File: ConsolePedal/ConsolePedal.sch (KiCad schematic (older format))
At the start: 1 part, among them U1 N64-Cartridge

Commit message: Finished schematic
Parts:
- added BT1: Battery, symbol Device:Battery
- added D1: LED, LED_THT:LED_D5.0mm, symbol Device:LED
- added J1: AudioJack3, Connector_PinSocket_2.54mm:PinSocket_1x03_P2.54mm_Vertical, symbol audioJacks:AudioJack3
- added J2: AudioJack2, Connector_PinSocket_2.54mm:PinSocket_1x02_P2.54mm_Vertical, symbol audioJacks:AudioJack2
- added R1: R, Resistor_THT:R_Axial_DIN0207_L6.3mm_D2.5mm_P10.16mm_Horizontal, symbol Device:R
- added S1: SWITCH-3PDT-PTH-STOMP, MuffPi:STOMP_SWITCH_3PDT, symbol SparkFun-Switches:SWITCH-3PDT-PTH-STOMP
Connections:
- net GND: now reaches U1.1 (GND)
- net GND: now also U1.2 (GND), U1.49 (RAUDIO), U1.50 (GND), J1.1, J2.2, R1.2
- net Input: now reaches U1.3 (AD15)
- net Input: now also U1.48 (GND), S1.P$3 (S)
- net Output: now reaches U1.4 (AD14)
- net Output: now also U1.47 (GND), S1.P$6 (S)
- net LEDPower: now reaches U1.45 (os_event_cart)
- net LEDPower: now also U1.6 (GND), D1.2 (A), S1.P$9 (S)
- net +9V: now reaches U1.46 (NC)
- net +9V: now also U1.5 (AD13), BT1.1 (+), S1.P$8 (P)
- new net: J2.1, S1.P$5 (P)
- new net: BT1.2 (-), J1.2
- new net: J1.3, S1.P$2 (P)
- new net: S1.P$1 (O), S1.P$4 (O)
- new net: D1.1 (K), R1.1
- no-connect marks 0 -> 1
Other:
- moved on the sheet: U1

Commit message: Finalized board layout. Working on pcb graphics
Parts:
- removed U1: N64-Cartridge, Connector_PinSocket_2.54mm:PinSocket_2x25_P2.54mm_Vertical, symbol n64-cartridge:N64-Cartridge
- added J3: Conn_02x25_Odd_Even, Connector_PinSocket_2.54mm:PinSocket_2x25_P2.54mm_Vertical, symbol Connector_Generic:Conn_02x25_Odd_Even
- BT1: footprint (none) -> Connector_PinSocket_2.54mm:PinSocket_1x02_P2.54mm_Vertical
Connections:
- net +9V: now also J3.10 (Pin_10), J3.41 (Pin_41), J3.42 (Pin_42), J3.9 (Pin_9)
- net GND: now also J3.1 (Pin_1), J3.2 (Pin_2), J3.3 (Pin_3), J3.4 (Pin_4), J3.47 (Pin_47), J3.48 (Pin_48), J3.49 (Pin_49), J3.50 (Pin_50)
- net Input: now also J3.45 (Pin_45), J3.46 (Pin_46), J3.5 (Pin_5), J3.6 (Pin_6)
- net LEDPower: now also J3.11 (Pin_11), J3.12 (Pin_12), J3.39 (Pin_39), J3.40 (Pin_40)
- net Output: now also J3.43 (Pin_43), J3.44 (Pin_44), J3.7 (Pin_7), J3.8 (Pin_8)
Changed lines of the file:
@@
 F 0 "BT1" H 5458 1696 50  0000 L CNN
 F 1 "Battery" H 5458 1605 50  0000 L CNN
-F 2 "" V 5350 1710 50  0001 C CNN
+F 2 "Connector_PinSocket_2.54mm:PinSocket_1x02_P2.54mm_Vertical" V 5350 1710 50  0001 C CNN
 F 3 "~" V 5350 1710 50  0001 C CNN
 	1    5350 1650
@@
 	8250 1550 8250 1650
 $Comp
-L power:GND #PWR09
-U 1 1 5FA91B35
-P 10450 3950
-F 0 "#PWR09" H 10450 3700 50  0001 C CNN
-F 1 "GND" H 10455 3777 50  0000 C CNN
-F 2 "" H 10450 3950 50  0001 C CNN
-F 3 "" H 10450 3950 50  0001 C CNN
-	1    10450 3950
-	1    0    0    -1
-$EndComp
-Wire Wire Line
-	10300 3950 10450 3950
-Wire Wire Line
-	10300 3850 10300 3950
-$Comp
 L power:GND #PWR06
 U 1 1 5FA92668
@@
 Wire Wire Line
 	7650 1550 8250 1550
-Text Label 10300 3750 0    50   ~ 0
-Input
-Text Label 10300 3650 0    50   ~ 0
-Output
 Text Label 8250 1750 2    50   ~ 0
 Input
@@
 	0    -1   -1   0
 $EndComp
-$Comp
-L power:+9V #PWR08
-U 1 1 5FA963AA
-P 10300 3550
-F 0 "#PWR08" H 10300 3400 50  0001 C CNN
-F 1 "+9V" V 10315 3678 50  0000 L CNN
-F 2 "" H 10300 3550 50  0001 C CNN
-F 3 "" H 10300 3550 50  0001 C CNN
-	1    10300 3550
-	0    1    1    0
-$EndComp
 Text Label 6800 3150 0    50   ~ 0
 LEDPower
@@
 Text Label 8250 2050 2    50   ~ 0
 LEDPower
-Text Label 10300 3450 0    50   ~ 0
+Text Label 8750 3450 0    50   ~ 0
 LEDPower
-Connection ~ 10300 3950
-Connection ~ 8250 1550
 $Comp
-L n64-cartridge:N64-Cartridge U1
-U 1 1 5FA742E9
-P 9300 3850
-F 0 "U1" H 9300 6350 60  0000 C CNN
-F 1 "N64-Cartridge" H 9300 6450 60  0000 C CNN
-F 2 "Connector_PinSocket_2.54mm:PinSocket_2x25_P2.54mm_Vertical" H 9250 3900 60  0001 C CNN
-F 3 "" H 9250 3900 60  0000 C CNN
-	1    9300 3850
+L power:+9V #PWR08
+U 1 1 5FA963AA
+P 8750 3550
+F 0 "#PWR08" H 8750 3400 50  0001 C CNN
+F 1 "+9V" V 8765 3678 50  0000 L CNN
+F 2 "" H 8750 3550 50  0001 C CNN
+F 3 "" H 8750 3550 50  0001 C CNN
+	1    8750 3550
+	0    1    1    0
+$EndComp
+Text Label 8750 3650 0    50   ~ 0
+Output
+Text Label 8750 3750 0    50   ~ 0
+Input
+Wire Wire Line
+	8750 3850 8750 3950
+Wire Wire Line
+	8750 3950 8900 3950
+$Comp
+L power:GND #PWR09
+U 1 1 5FA91B35
+P 8900 3950
+F 0 "#PWR09" H 8900 3700 50  0001 C CNN
+F 1 "GND" H 8905 3777 50  0000 C CNN
+F 2 "" H 8900 3950 50  0001 C CNN
+F 3 "" H 8900 3950 50  0001 C CNN
+	1    8900 3950
 	1    0    0    -1
 $EndComp
+$Comp
+L Connector_Generic:Conn_02x25_Odd_Even J3
+U 1 1 5FABBF0E
+P 8450 2750
+F 0 "J3" H 8500 4167 50  0000 C CNN
+F 1 "Conn_02x25_Odd_Even" H 8500 4076 50  0000 C CNN
+F 2 "Connector_PinSocket_2.54mm:PinSocket_2x25_P2.54mm_Vertical" H 8450 2750 50  0001 C CNN
+F 3 "~" H 8450 2750 50  0001 C CNN
+	1    8450 2750
+	1    0    0    -1
+$EndComp
+Connection ~ 8250 1550
+Connection ~ 8750 3950
+Wire Wire Line
+	8750 1650 8750 1550
+$Comp
+L power:GND #PWR0101
+U 1 1 5FACAD9C
+P 9200 1550
+F 0 "#PWR0101" H 9200 1300 50  0001 C CNN
+F 1 "GND" H 9205 1377 50  0000 C CNN
+F 2 "" H 9200 1550 50  0001 C CNN
+F 3 "" H 9200 1550 50  0001 C CNN
+	1    9200 1550
+	1    0    0    -1
+$EndComp
+Wire Wire Line
+	8750 1550 9200 1550
+Connection ~ 8750 1550
+Text Label 8750 1750 0    50   ~ 0
+Input
+Text Label 8750 1850 0    50   ~ 0
+Output
+$Comp
+L power:+9V #PWR0102
+U 1 1 5FACB96C
+P 8750 1950
+F 0 "#PWR0102" H 8750 1800 50  0001 C CNN
+F 1 "+9V" V 8765 2078 50  0000 L CNN
+F 2 "" H 8750 1950 50  0001 C CNN
+F 3 "" H 8750 1950 50  0001 C CNN
+	1    8750 1950
+	0    1    1    0
+$EndComp
+Text Label 8750 2050 0    50   ~ 0
+LEDPower
+Text Label 8250 3450 2    50   ~ 0
+LEDPower
+$Comp
+L power:+9V #PWR0103
+U 1 1 5FACC0AD
+P 8250 3550
+F 0 "#PWR0103" H 8250 3400 50  0001 C CNN
+F 1 "+9V" V 8265 3678 50  0000 L CNN
+F 2 "" H 8250 3550 50  0001 C CNN
+F 3 "" H 8250 3550 50  0001 C CNN
+	1    8250 3550
+	0    -1   -1   0
+$EndComp
+Text Label 8250 3650 2    50   ~ 0
+Output
+Text Label 8250 3750 2    50   ~ 0
+Input
+Wire Wire Line
+	8250 3850 8250 3950
+$Comp
+L power:GND #PWR0104
+U 1 1 5FACD3A0
+P 8100 3950
+F 0 "#PWR0104" H 8100 3700 50  0001 C CNN
+F 1 "GND" H 8105 3777 50  0000 C CNN
+F 2 "" H 8100 3950 50  0001 C CNN
+F 3 "" H 8100 3950 50  0001 C CNN
+	1    8100 3950
+	1    0    0    -1
+$EndComp
+Wire Wire Line
+	8100 3950 8250 3950
+Connection ~ 8250 3950
 $EndSCHEMATC

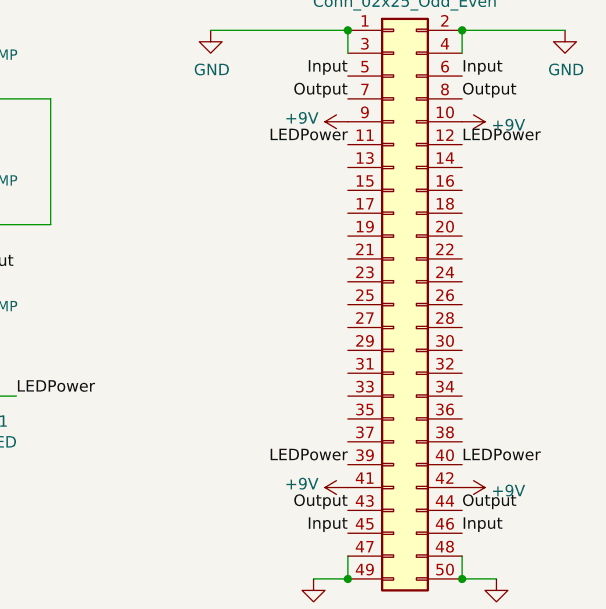
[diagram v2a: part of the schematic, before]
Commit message: Made n64 connector pins further apart to match real socket connector and moved led for easier mounting
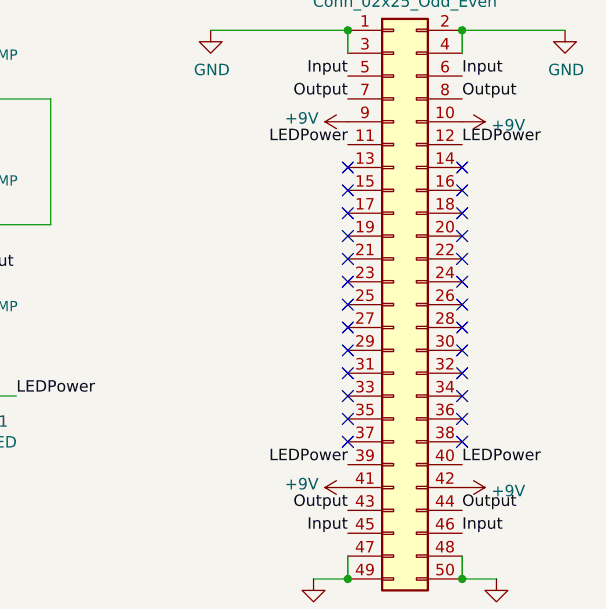
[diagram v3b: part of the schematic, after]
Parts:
- J3: footprint Connector_PinSocket_2.54mm:PinSocket_2x25_P2.54mm_Vertical -> libraries:n64Socket
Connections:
- no-connect marks 1 -> 27
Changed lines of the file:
@@
 F 0 "J3" H 8500 4167 50  0000 C CNN
 F 1 "Conn_02x25_Odd_Even" H 8500 4076 50  0000 C CNN
-F 2 "Connector_PinSocket_2.54mm:PinSocket_2x25_P2.54mm_Vertical" H 8450 2750 50  0001 C CNN
+F 2 "libraries:n64Socket" H 8450 2750 50  0001 C CNN
 F 3 "~" H 8450 2750 50  0001 C CNN
 	1    8450 2750
@@
 	8100 3950 8250 3950
 Connection ~ 8250 3950
+NoConn ~ 8750 2150
+NoConn ~ 8750 2250
+NoConn ~ 8750 2350
+NoConn ~ 8750 2450
+NoConn ~ 8750 2550
+NoConn ~ 8750 2650
+NoConn ~ 8750 2750
+NoConn ~ 8750 2850
+NoConn ~ 8750 2950
+NoConn ~ 8750 3050
+NoConn ~ 8750 3150
+NoConn ~ 8750 3250
+NoConn ~ 8750 3350
+NoConn ~ 8250 3350
+NoConn ~ 8250 3250
+NoConn ~ 8250 3150
+NoConn ~ 8250 3050
+NoConn ~ 8250 2950
+NoConn ~ 8250 2850
+NoConn ~ 8250 2750
+NoConn ~ 8250 2650
+NoConn ~ 8250 2550
+NoConn ~ 8250 2450
+NoConn ~ 8250 2350
+NoConn ~ 8250 2250
+NoConn ~ 8250 2150
 $EndSCHEMATC

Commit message: Moving polarity protection diode to mainboard so each cartridge doesn't need to have its own
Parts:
- added D2: D, Diode_THT:D_DO-41_SOD81_P10.16mm_Horizontal, symbol Device:D
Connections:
- net +9V: now also D2.1 (K); no longer BT1.1 (+)
- new net: BT1.1 (+), D2.2 (A)
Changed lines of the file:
@@
 L power:+9V #PWR02
 U 1 1 5FA8F935
-P 5350 1450
-F 0 "#PWR02" H 5350 1300 50  0001 C CNN
-F 1 "+9V" H 5365 1623 50  0000 C CNN
-F 2 "" H 5350 1450 50  0001 C CNN
-F 3 "" H 5350 1450 50  0001 C CNN
-	1    5350 1450
+P 5800 1350
+F 0 "#PWR02" H 5800 1200 50  0001 C CNN
+F 1 "+9V" H 5815 1523 50  0000 C CNN
+F 2 "" H 5800 1350 50  0001 C CNN
+F 3 "" H 5800 1350 50  0001 C CNN
+	1    5800 1350
 	1    0    0    -1
 $EndComp
@@
 NoConn ~ 8250 2250
 NoConn ~ 8250 2150
+$Comp
+L Device:D D2
+U 1 1 601EEB67
+P 5500 1350
+F 0 "D2" H 5500 1133 50  0000 C CNN
+F 1 "D" H 5500 1224 50  0000 C CNN
+F 2 "Diode_THT:D_DO-41_SOD81_P10.16mm_Horizontal" H 5500 1350 50  0001 C CNN
+F 3 "~" H 5500 1350 50  0001 C CNN
+	1    5500 1350
+	-1   0    0    1
+$EndComp
+Wire Wire Line
+	5350 1450 5350 1350
+Wire Wire Line
+	5800 1350 5650 1350
 $EndSCHEMATC
